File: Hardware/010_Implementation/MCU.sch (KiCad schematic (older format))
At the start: 16 parts, among them J4 Conn_02x05_Odd_Even, SW1 SW_Push, U14 ESP32-DEVKITC-32D, X1 2716-106

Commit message: Changes to Schematic. Button, LEDs and Power Flags
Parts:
- D3: value LED -> RED; footprint LED_SMD:LED_1806_4516Metric_Pad1.57x1.80mm_HandSolder -> (none)
- D4, D5: value LED -> GREEN; footprint LED_SMD:LED_1806_4516Metric_Pad1.57x1.80mm_HandSolder -> (none)
- R10: value 220 -> 2.2K
- R15, R16, R17: value 220 -> R; footprint Resistor_SMD:R_2512_6332Metric_Pad1.52x3.35mm_HandSolder -> (none)
- renumbered J4 to J3
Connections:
- net labels added: +3.3V, Indicator_AP_Mode, Indicator_Error, Indicator_STA_Mode
- net labels removed: 3.3V, Ind_AP_Mode, Ind_Error, Ind_STA_Mode, VCC
- wire segments 104 -> 73
- no-connect marks 20 -> 37
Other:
- moved on the sheet: C7, R10, SW1

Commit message: Updated Schematic. Fixed Connection to Ground to prevent Software Bugs
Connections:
- wire segments 73 -> 77
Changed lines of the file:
@@
 L power:GND #PWR05
 U 1 1 5F86D925
-P 1950 2875
-F 0 "#PWR05" H 1950 2625 50  0001 C CNN
-F 1 "GND" H 1955 2702 50  0000 C CNN
-F 2 "" H 1950 2875 50  0001 C CNN
-F 3 "" H 1950 2875 50  0001 C CNN
-	1    1950 2875
+P 1950 2925
+F 0 "#PWR05" H 1950 2675 50  0001 C CNN
+F 1 "GND" H 1955 2752 50  0000 C CNN
+F 2 "" H 1950 2925 50  0001 C CNN
+F 3 "" H 1950 2925 50  0001 C CNN
+	1    1950 2925
 	1    0    0    -1
 $EndComp
@@
 L power:GND #PWR06
 U 1 1 5F875863
-P 5400 2175
-F 0 "#PWR06" H 5400 1925 50  0001 C CNN
-F 1 "GND" H 5405 2002 50  0000 C CNN
-F 2 "" H 5400 2175 50  0001 C CNN
-F 3 "" H 5400 2175 50  0001 C CNN
-	1    5400 2175
+P 5400 2200
+F 0 "#PWR06" H 5400 1950 50  0001 C CNN
+F 1 "GND" H 5405 2027 50  0000 C CNN
+F 2 "" H 5400 2200 50  0001 C CNN
+F 3 "" H 5400 2200 50  0001 C CNN
+	1    5400 2200
 	1    0    0    -1
 $EndComp
@@
 L power:GND #PWR07
 U 1 1 5F8A2636
-P 8350 3100
-F 0 "#PWR07" H 8350 2850 50  0001 C CNN
-F 1 "GND" H 8355 2927 50  0000 C CNN
-F 2 "" H 8350 3100 50  0001 C CNN
-F 3 "" H 8350 3100 50  0001 C CNN
-	1    8350 3100
+P 8350 3150
+F 0 "#PWR07" H 8350 2900 50  0001 C CNN
+F 1 "GND" H 8355 2977 50  0000 C CNN
+F 2 "" H 8350 3150 50  0001 C CNN
+F 3 "" H 8350 3150 50  0001 C CNN
+	1    8350 3150
 	1    0    0    -1
 $EndComp
@@
 	3050 6125 3050 6300
 Wire Wire Line
-	3050 6300 3350 6300
-Wire Wire Line
 	3675 6300 3675 6050
 Wire Wire Line
@@
 L power:GND #PWR0101
 U 1 1 5F8F6B0F
-P 3350 6300
-F 0 "#PWR0101" H 3350 6050 50  0001 C CNN
-F 1 "GND" H 3355 6127 50  0000 C CNN
-F 2 "" H 3350 6300 50  0001 C CNN
-F 3 "" H 3350 6300 50  0001 C CNN
-	1    3350 6300
-	1    0    0    -1
-$EndComp
-Connection ~ 3350 6300
-Wire Wire Line
-	3350 6300 3675 6300
+P 3350 6350
+F 0 "#PWR0101" H 3350 6100 50  0001 C CNN
+F 1 "GND" H 3355 6177 50  0000 C CNN
+F 2 "" H 3350 6350 50  0001 C CNN
+F 3 "" H 3350 6350 50  0001 C CNN
+	1    3350 6350
+	1    0    0    -1
+$EndComp
 $Comp
 L power:+3.3V #PWR0102
@@
 Entry Wire Line
 	1600 2675 1700 2575
-Wire Bus Line
-	1600 2375 1600 5875
 $Comp
 L power:+3.3V #PWR0103
@@
 	1    0    0    -1
 $EndComp
+Wire Wire Line
+	3050 6300 3350 6300
+Wire Wire Line
+	3350 6350 3350 6300
+Connection ~ 3350 6300
+Wire Wire Line
+	3350 6300 3675 6300
+Wire Wire Line
+	5400 2200 5400 2175
+Wire Wire Line
+	1950 2875 1950 2925
+Wire Wire Line
+	8350 3150 8350 3100
+Wire Bus Line
+	1600 2375 1600 5875
 $EndSCHEMATC

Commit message: Modified Board Schematic. Optimized supply and switching system through Software
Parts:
- removed R10: 2.2K, Resistor_SMD:R_2512_6332Metric_Pad1.52x3.35mm_HandSolder, symbol Device:R
- added D3: SS24, Board:DIOM5336X265N, symbol Board:SS24
- added R5: 2.2k, Resistor_SMD:R_0805_2012Metric_Pad1.15x1.40mm_HandSolder, symbol Device:R
- D4: renamed from D3; footprint (none) -> LED_THT:LED_D3.0mm
- D5: renamed from D4; footprint (none) -> LED_THT:LED_D3.0mm
- D6: renamed from D5; footprint (none) -> LED_THT:LED_D3.0mm
- R10: renamed from R15; value R -> 500; footprint (none) -> Resistor_SMD:R_0805_2012Metric_Pad1.15x1.40mm_HandSolder
- R11: renamed from R16; value R -> 500; footprint (none) -> Resistor_SMD:R_0805_2012Metric_Pad1.15x1.40mm_HandSolder
- R12: renamed from R17; value R -> 500; footprint (none) -> Resistor_SMD:R_0805_2012Metric_Pad1.15x1.40mm_HandSolder
- R6: renamed from R11; footprint Resistor_SMD:R_2512_6332Metric_Pad1.52x3.35mm_HandSolder -> Resistor_SMD:R_0805_2012Metric_Pad1.15x1.40mm_HandSolder
- R7: renamed from R12; footprint Resistor_SMD:R_2512_6332Metric_Pad1.52x3.35mm_HandSolder -> Resistor_SMD:R_0805_2012Metric_Pad1.15x1.40mm_HandSolder
- R8: renamed from R13; footprint Resistor_SMD:R_2512_6332Metric_Pad1.52x3.35mm_HandSolder -> Resistor_SMD:R_0805_2012Metric_Pad1.15x1.40mm_HandSolder
- R9: renamed from R14; footprint Resistor_SMD:R_2512_6332Metric_Pad1.52x3.35mm_HandSolder -> Resistor_SMD:R_0805_2012Metric_Pad1.15x1.40mm_HandSolder
- renumbered J3 to J1, U14 to U2
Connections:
- net labels added: Ext.5V, OBD-CAN_Switch, OBD_Voltage_Check
- net labels removed: EN_CAN, EN_Transceiver, USB_GND, USB_VDD
- wire segments 77 -> 80
- no-connect marks 37 -> 36
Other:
- moved on the sheet: C7, SW1

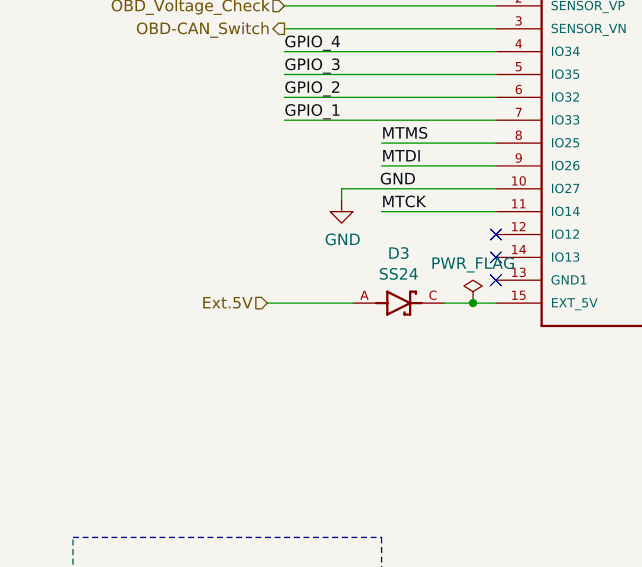
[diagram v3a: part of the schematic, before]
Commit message: Added Missing 5V marker
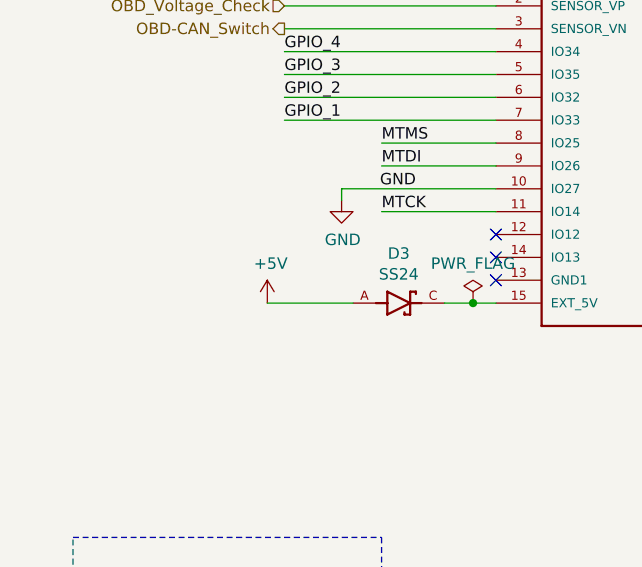
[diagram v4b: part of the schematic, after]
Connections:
- net labels added: +5V
- net labels removed: Ext.5V
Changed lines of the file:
@@
 Wire Wire Line
 	1850 1575 2175 1575
-Text HLabel 1625 3375 0    50   Input ~ 0
-Ext.5V
 $Comp
 L power:PWR_FLAG #FLG02
@@
 Wire Wire Line
 	2525 3375 2625 3375
+$Comp
+L power:+5V #PWR?
+U 1 1 5FA19D37
+P 1625 3375
+F 0 "#PWR?" H 1625 3225 50  0001 C CNN
+F 1 "+5V" H 1640 3548 50  0000 C CNN
+F 2 "" H 1625 3375 50  0001 C CNN
+F 3 "" H 1625 3375 50  0001 C CNN
+	1    1625 3375
+	1    0    0    -1
+$EndComp
 $EndSCHEMATC

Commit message: PCB Updated
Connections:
- wire segments 80 -> 82
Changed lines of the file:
@@
 L power:+3.3V #PWR07
 U 1 1 5F86D27D
-P 1925 5025
-F 0 "#PWR07" H 1925 4875 50  0001 C CNN
-F 1 "+3.3V" H 1940 5198 50  0000 C CNN
-F 2 "" H 1925 5025 50  0001 C CNN
-F 3 "" H 1925 5025 50  0001 C CNN
-	1    1925 5025
+P 1925 4975
+F 0 "#PWR07" H 1925 4825 50  0001 C CNN
+F 1 "+3.3V" H 1940 5148 50  0000 C CNN
+F 2 "" H 1925 4975 50  0001 C CNN
+F 3 "" H 1925 4975 50  0001 C CNN
+	1    1925 4975
 	1    0    0    -1
 $EndComp
@@
 L power:GND #PWR015
 U 1 1 5F90B7D2
-P 9725 4825
-F 0 "#PWR015" H 9725 4575 50  0001 C CNN
-F 1 "GND" H 9730 4652 50  0000 C CNN
-F 2 "" H 9725 4825 50  0001 C CNN
-F 3 "" H 9725 4825 50  0001 C CNN
-	1    9725 4825
+P 9725 4875
+F 0 "#PWR015" H 9725 4625 50  0001 C CNN
+F 1 "GND" H 9730 4702 50  0000 C CNN
+F 2 "" H 9725 4875 50  0001 C CNN
+F 3 "" H 9725 4875 50  0001 C CNN
+	1    9725 4875
 	1    0    0    -1
 $EndComp
@@
 	2525 3375 2625 3375
 $Comp
-L power:+5V #PWR?
+L power:+5V #PWR022
 U 1 1 5FA19D37
 P 1625 3375
-F 0 "#PWR?" H 1625 3225 50  0001 C CNN
+F 0 "#PWR022" H 1625 3225 50  0001 C CNN
 F 1 "+5V" H 1640 3548 50  0000 C CNN
 F 2 "" H 1625 3375 50  0001 C CNN
@@
 	1    0    0    -1
 $EndComp
+Wire Wire Line
+	1925 4975 1925 5025
+Wire Wire Line
+	9725 4825 9725 4875
 $EndSCHEMATC

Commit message: Board version 4
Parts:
- removed X1: 2716-106, Board:P-2716-106, symbol Board:2716-106
- added J1: 2606-3356, Board:2606-3356, symbol 2020-11-09_14-09-29:2606-3356
- C8: renamed from C7; footprint Capacitor_SMD:C_1812_4532Metric_Pad1.30x3.40mm_HandSolder -> Capacitor_SMD:C_0603_1608Metric_Pad1.05x0.95mm_HandSolder
- renumbered D3 to D2, D4 to D3, D5 to D4, D6 to D5, J1 to J2, R7 to R10, R8 to R11, R9 to R12, R10 to R13, R11 to R14, R12 to R15, R5 to R8, R6 to R9
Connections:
- no-connect marks 36 -> 17
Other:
- moved on the sheet: D2, U2

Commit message: Board version 4.1
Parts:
- J1: symbol 2020-11-09_14-09-29:2606-3356 -> Board-rescue:2606-3356-2020-11-09_14-09-29
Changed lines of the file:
@@
 	4100 3350 5025 3350
 $Comp
-L 2020-11-09_14-09-29:2606-3356 J1
+L Board-rescue:2606-3356-2020-11-09_14-09-29 J1
 U 1 1 5FB5C146
 P 1325 6275
+AR Path="/5FB5C146" Ref="J1"  Part="1"
+AR Path="/5F52F099/5FB5C146" Ref="J1"  Part="1"
 F 0 "J1" H 1567 4888 60  0000 C CNN
 F 1 "2606-3356" H 1567 4994 60  0000 C CNN

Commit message: Board Version 4.2
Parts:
- added C12, C15: 1u, symbol Device:C
- added C13, C14: 100n, symbol Device:C
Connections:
- net +3V3: now also C14.2, C15.2
- net GND: now also C12.2, C13.1, C14.1, C15.1
- net at D2.C, U2.15 (EXT_5V): now also C12.1, C13.2
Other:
- moved on the sheet: D2, U2
